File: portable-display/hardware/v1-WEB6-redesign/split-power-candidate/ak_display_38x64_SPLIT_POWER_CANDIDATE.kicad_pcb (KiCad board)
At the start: 4 copper layers, 38 x 64 mm, 120 parts, among them J1 USB4105-GF-A-060, J2 1S LiPo + NTC, J3 DEBUG POGO, J4 KD024EGOIN152-01, J5 MicroSD, Q1 2N7002, Q2 2N7002, Q3 AO3401A, SW1 UP, SW2 DOWN, SW3 OK, SW4 BACK, SW5 POWER, SW6 FEL, U1 AXP2101, U10 TPS65631DPDR, U2 V851s, U4 LIS2DW12TR, U5 RV-3028-C7, U6 SN74LVC1G123DCTR, U8 TPS22918DBVR, U9 USBLC6-2SC6, Y1 24MHz 10ppm

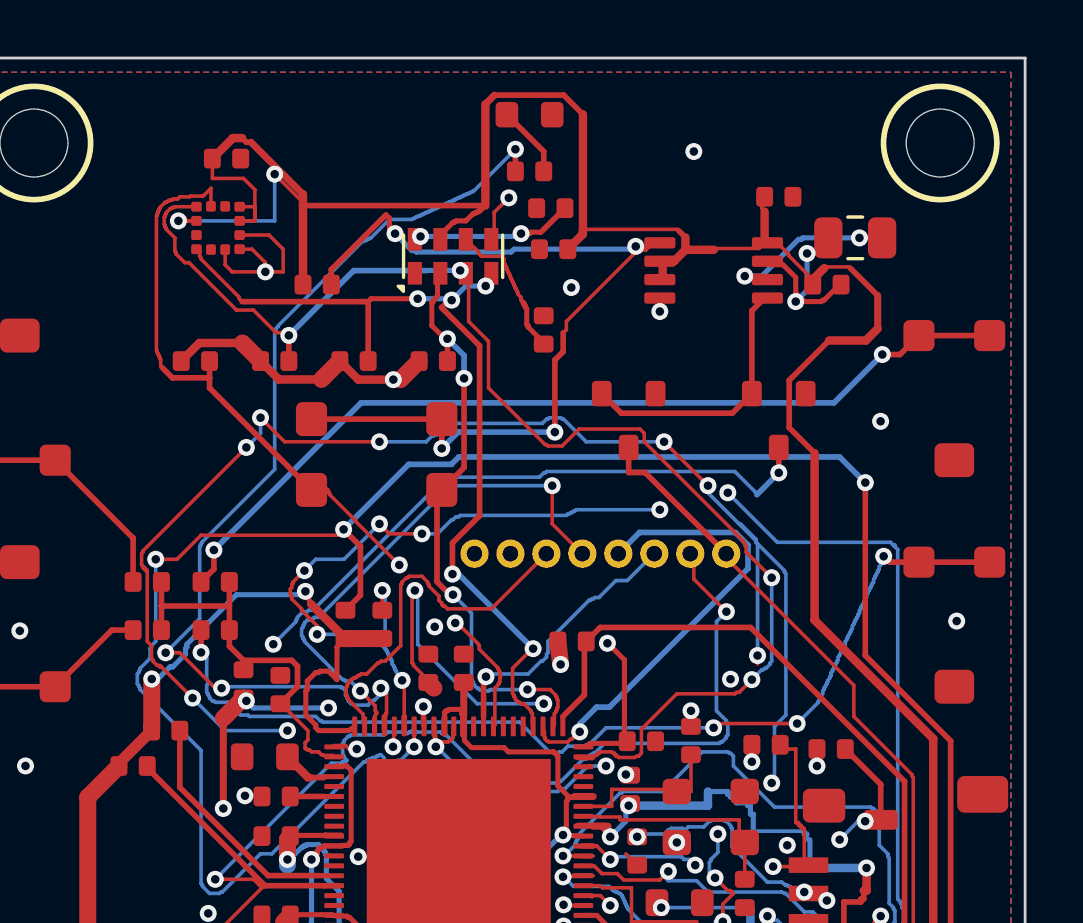
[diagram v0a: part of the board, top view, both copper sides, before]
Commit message: feat: add split power candidate hardware design and wake domain verification reports
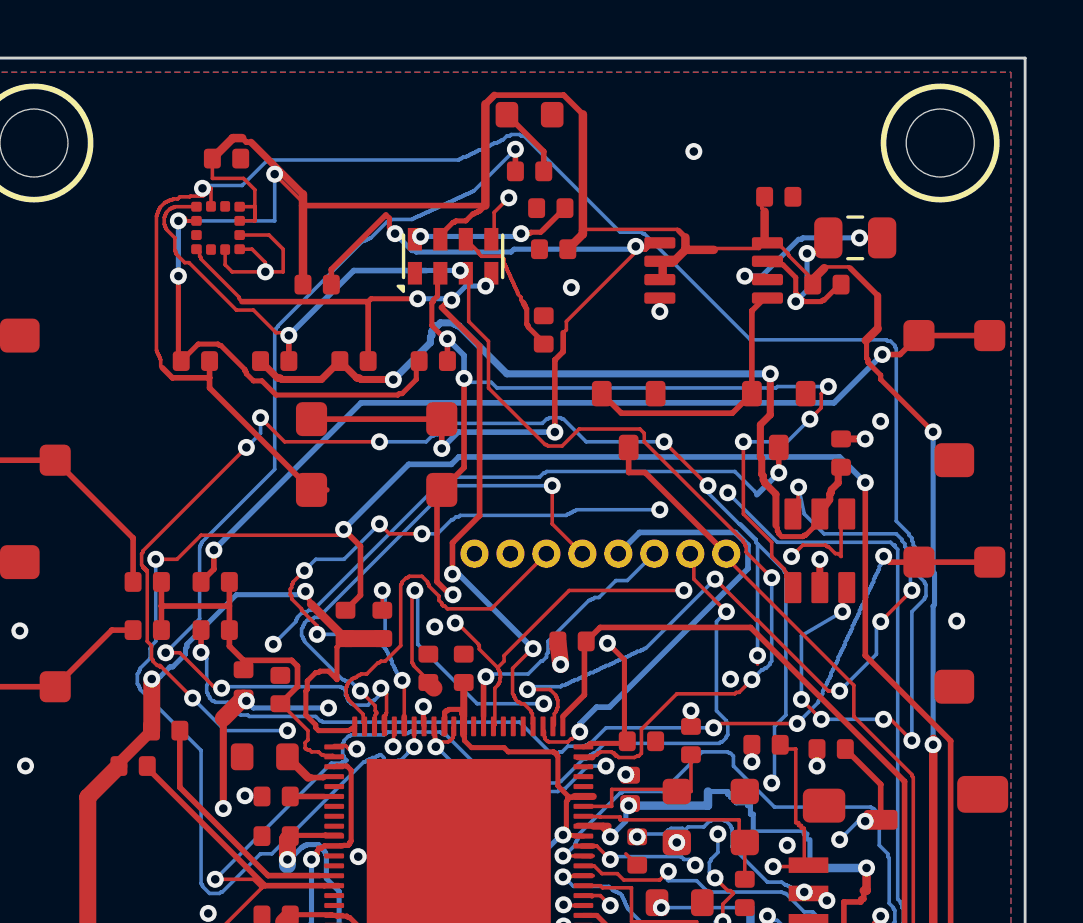
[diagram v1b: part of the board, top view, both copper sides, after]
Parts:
- added C52: 100n, Sameat:0402, F.Cu at (31.5, 13.9)
- added U11: SN74LVC2G17DBVR, Sameat:SN74LVC2G17_DBV6, F.Cu at (30.8, 17.4)
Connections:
- R17 pad 1: 3V3 -> RTC_3V3
- R18 pad 1: 3V3 -> RTC_3V3
- U2 pad 24: RTC_INT_N -> RTC_INT_SOC_N
- U2 pad 30: ACCEL_INT_N -> ACCEL_INT_SOC_N
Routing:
- net ACCEL_INT_N: track 28.2 -> 69.5 mm, vias 2 -> 6
- net RTC_INT_SOC_N: track 0.00 -> 29.0 mm, vias 0 -> 6
- net 3V3: track 137.2 -> 158.1 mm, vias 15 -> 16
- net ACCEL_INT_SOC_N: track 0.00 -> 20.5 mm, vias 0 -> 3
- net RTC_INT_N: track 21.3 -> 36.5 mm, vias 4 -> 6
- net RTC_3V3: track 117.8 -> 130.5 mm, vias 4 -> 7
- net GND: track 11.6 -> 13.5 mm, vias 56 -> 58

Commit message: review
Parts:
- added R33: 1k, Sameat:0402, F.Cu at (7.40, 28.9)
- added R34: 10k, Sameat:0402, F.Cu at (7.40, 27.6)
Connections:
- J3 pad 7: BOOT0 -> FEL_KEY_N
- SW6 pad 1: BOOT0 -> FEL_KEY_N
- SW6 pad 2: BOOT0 -> FEL_KEY_N
- U2 pad 56: unconnected-(U2-PC1_SPI0_CS-Pad56) -> FEL_N
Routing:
- net BOOT0: track 73.8 -> 8.55 mm, vias 2 -> 0
- net FEL_KEY_N: track 0.00 -> 62.7 mm, vias 0 -> 2
- net FEL_N: track 0.00 -> 0.72 mm, vias 0 -> 1

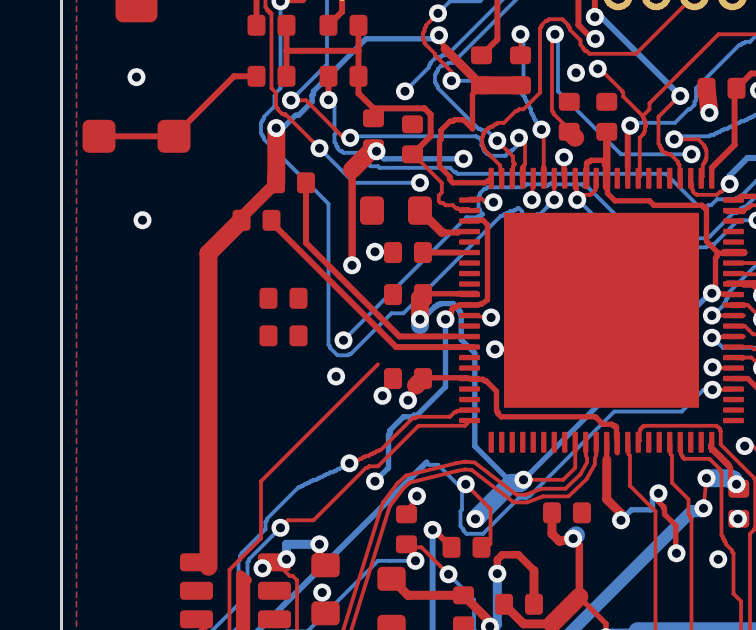
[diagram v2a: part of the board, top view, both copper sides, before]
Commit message: fix(pcb): complete FEL recovery copper (SW6/J3.7 -> R33 -> U2.56/PC1, R34 to 3V3)
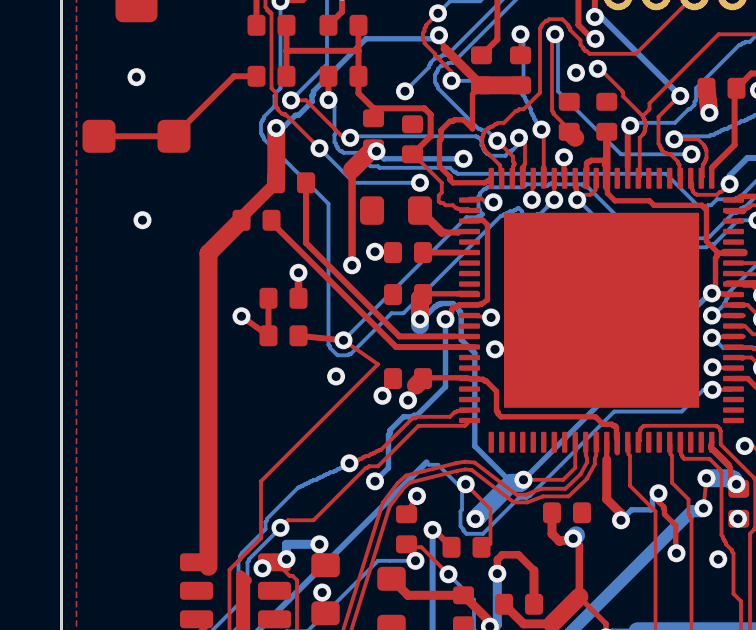
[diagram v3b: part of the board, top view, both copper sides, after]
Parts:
- turned R33 to 180 degrees
- turned R34 to 180 degrees
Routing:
- net FEL_N: track 0.72 -> 11.8 mm, vias 1 -> 2
- net FEL_KEY_N: track 62.7 -> 65.6 mm
- net 3V3: track 158.1 -> 159.0 mm, vias 16 -> 17

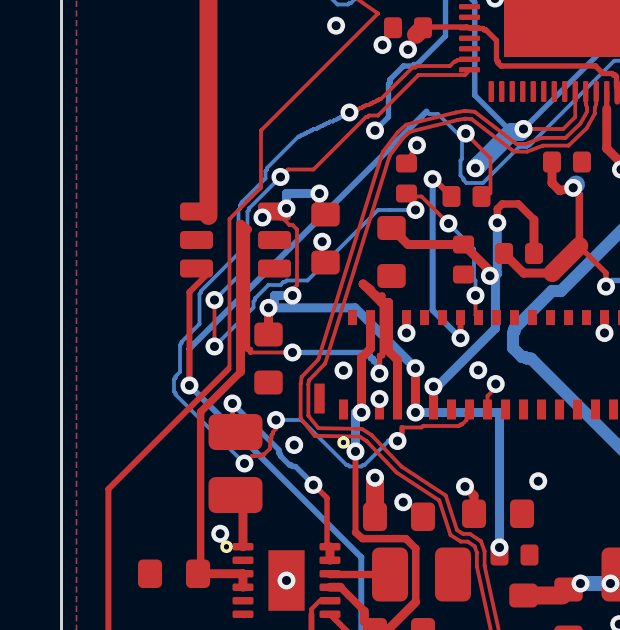
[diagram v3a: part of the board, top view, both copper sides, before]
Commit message: fix(pcb): add R35 10k LCD_EN pulldown for default-off display power
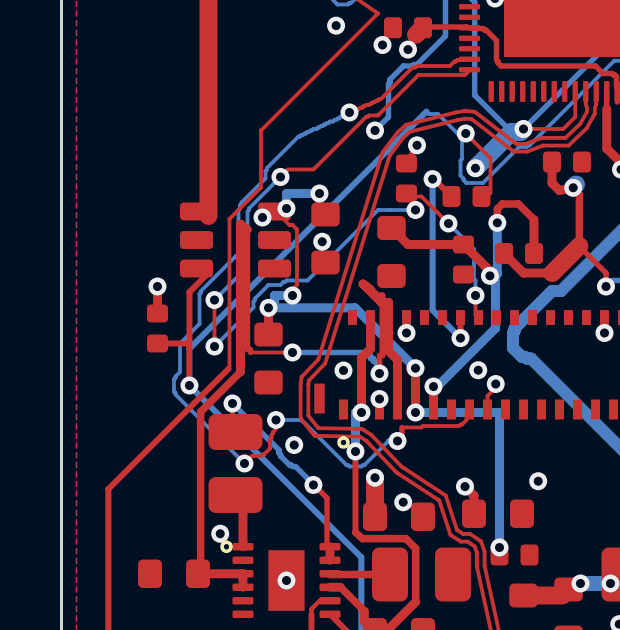
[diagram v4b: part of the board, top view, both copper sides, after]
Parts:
- added R35: 10k, Sameat:0402, F.Cu at (3.20, 40.3)
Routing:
- net LCD_EN: track 49.5 -> 50.5 mm
- net GND: track 13.5 -> 14.4 mm, vias 58 -> 59

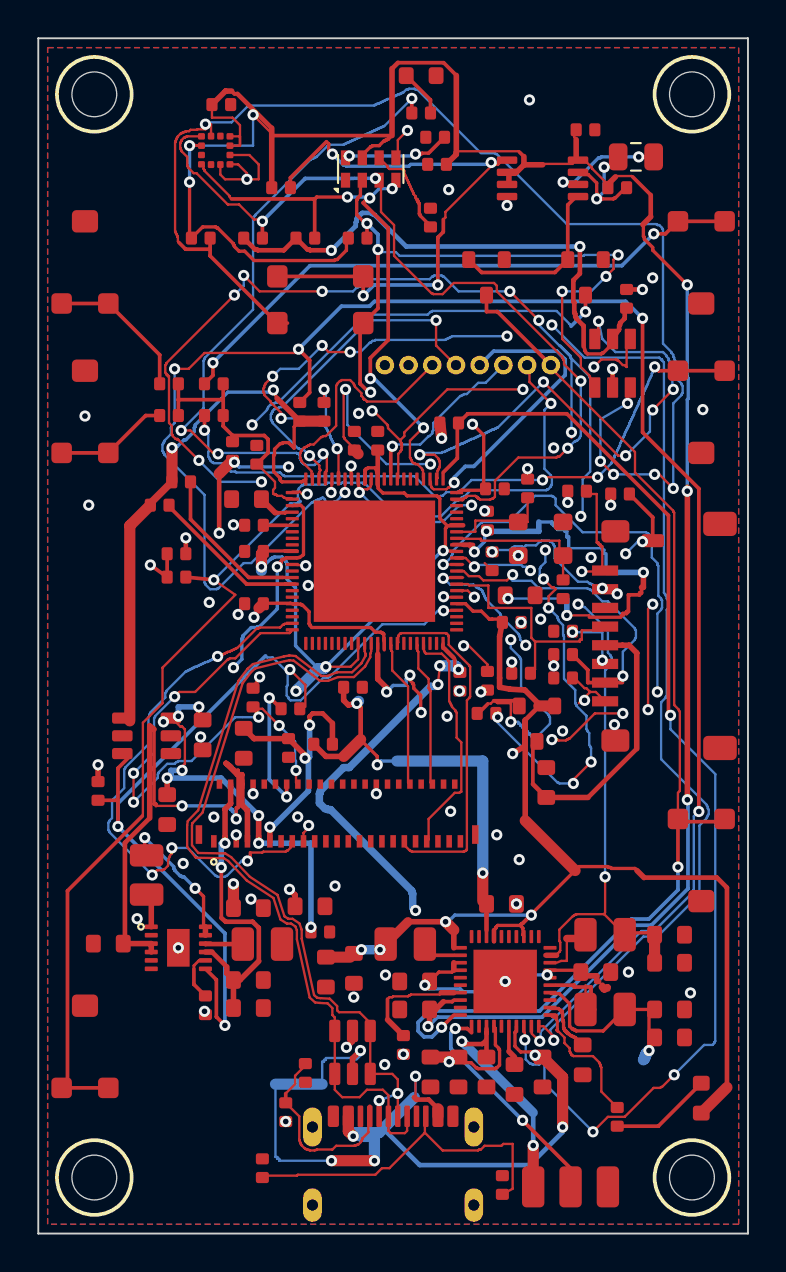
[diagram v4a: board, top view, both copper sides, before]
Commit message: fix(pcb): replace D6-D14 with ESDLC5V0LB (C20168172) on dedicated DFN1006-2 land
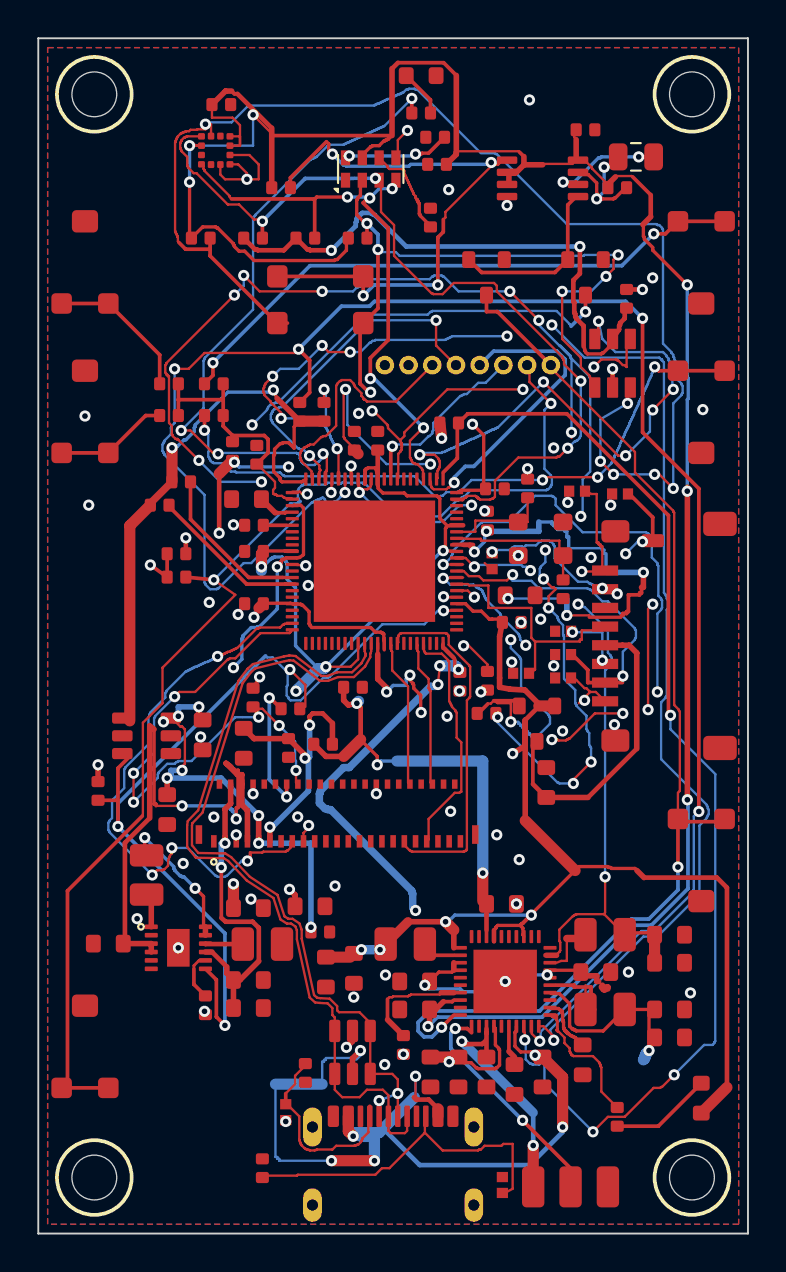
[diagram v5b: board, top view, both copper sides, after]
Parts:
- D10, D11, D12, D13, D14, D6, D7, D8, D9: value PESD4V0 -> ESDLC5V0LB; footprint Sameat:0402 -> Sameat:DFN1006-2
